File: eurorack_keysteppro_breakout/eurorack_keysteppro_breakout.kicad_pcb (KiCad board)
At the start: 2 copper layers, 25 parts, among them J1 AudioJack2_SwitchT, J10 AudioJack2_SwitchT, J11 AudioJack2_SwitchT, J12 AudioJack2_SwitchT, J13 AudioJack2_SwitchT, J14 AudioJack2_SwitchT, J15 AudioJack2_SwitchT, J16 AudioJack2_SwitchT, J17 AudioJack2_SwitchT, J18 Conn_02x08_Top_Bottom, J19 AudioJack2_SwitchT, J2 AudioJack2_SwitchT, J20 AudioJack2_SwitchT, J21 AudioJack2_SwitchT, J22 AudioJack2_SwitchT, J23 Conn_02x08_Top_Bottom, J24 AudioJack2_SwitchT, J25 AudioJack2_SwitchT, J3 AudioJack2_SwitchT, J4 AudioJack2_SwitchT, J5 AudioJack2_SwitchT, J6 AudioJack2_SwitchT, J7 AudioJack2_SwitchT, J8 AudioJack2_SwitchT, J9 AudioJack2_SwitchT

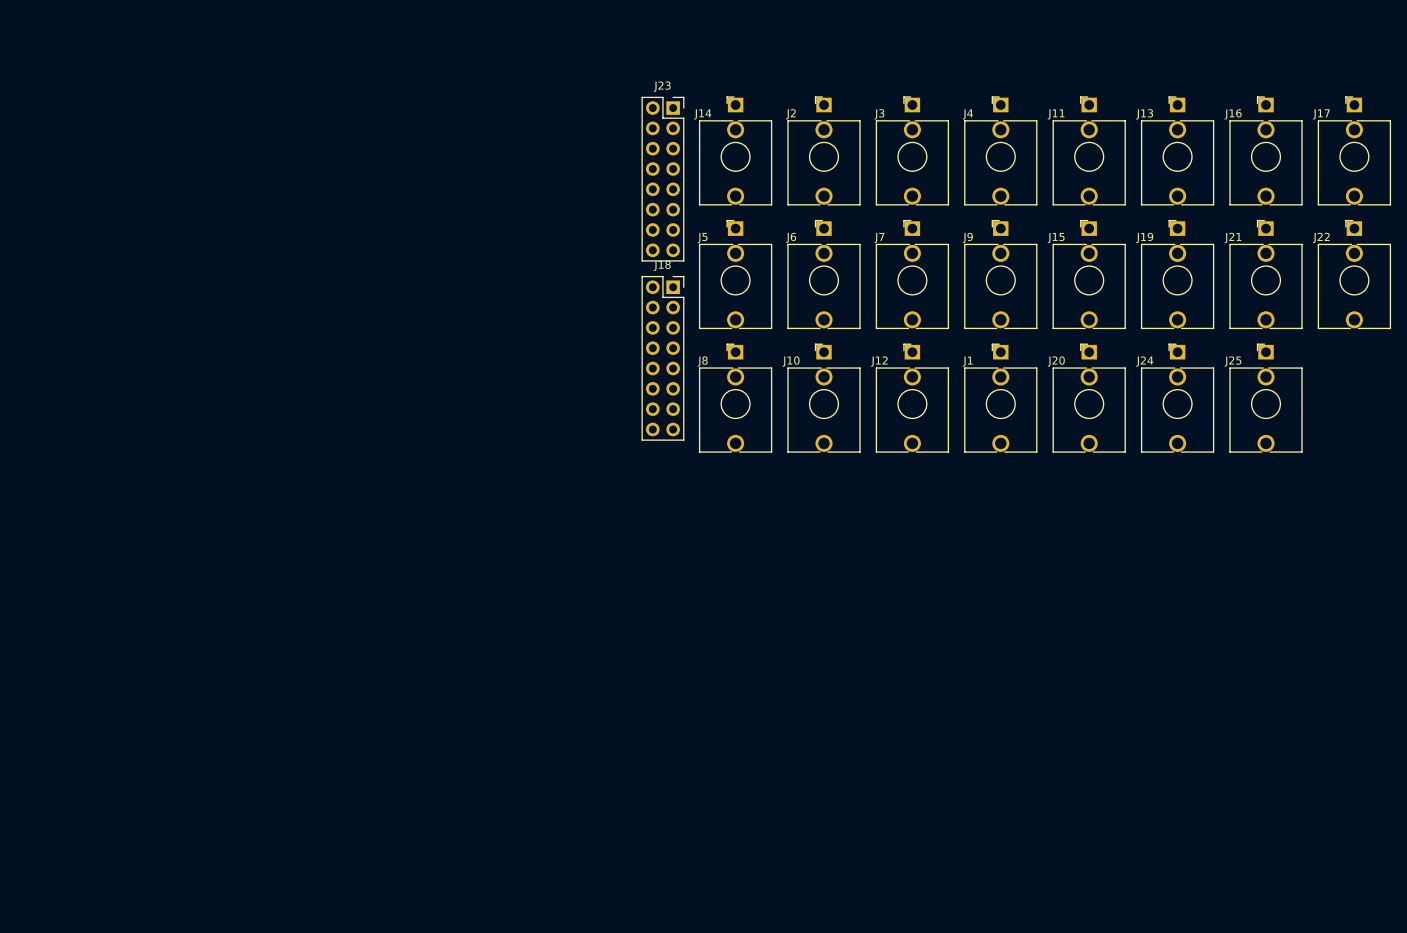
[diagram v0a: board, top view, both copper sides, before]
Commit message: roughly layout connectors
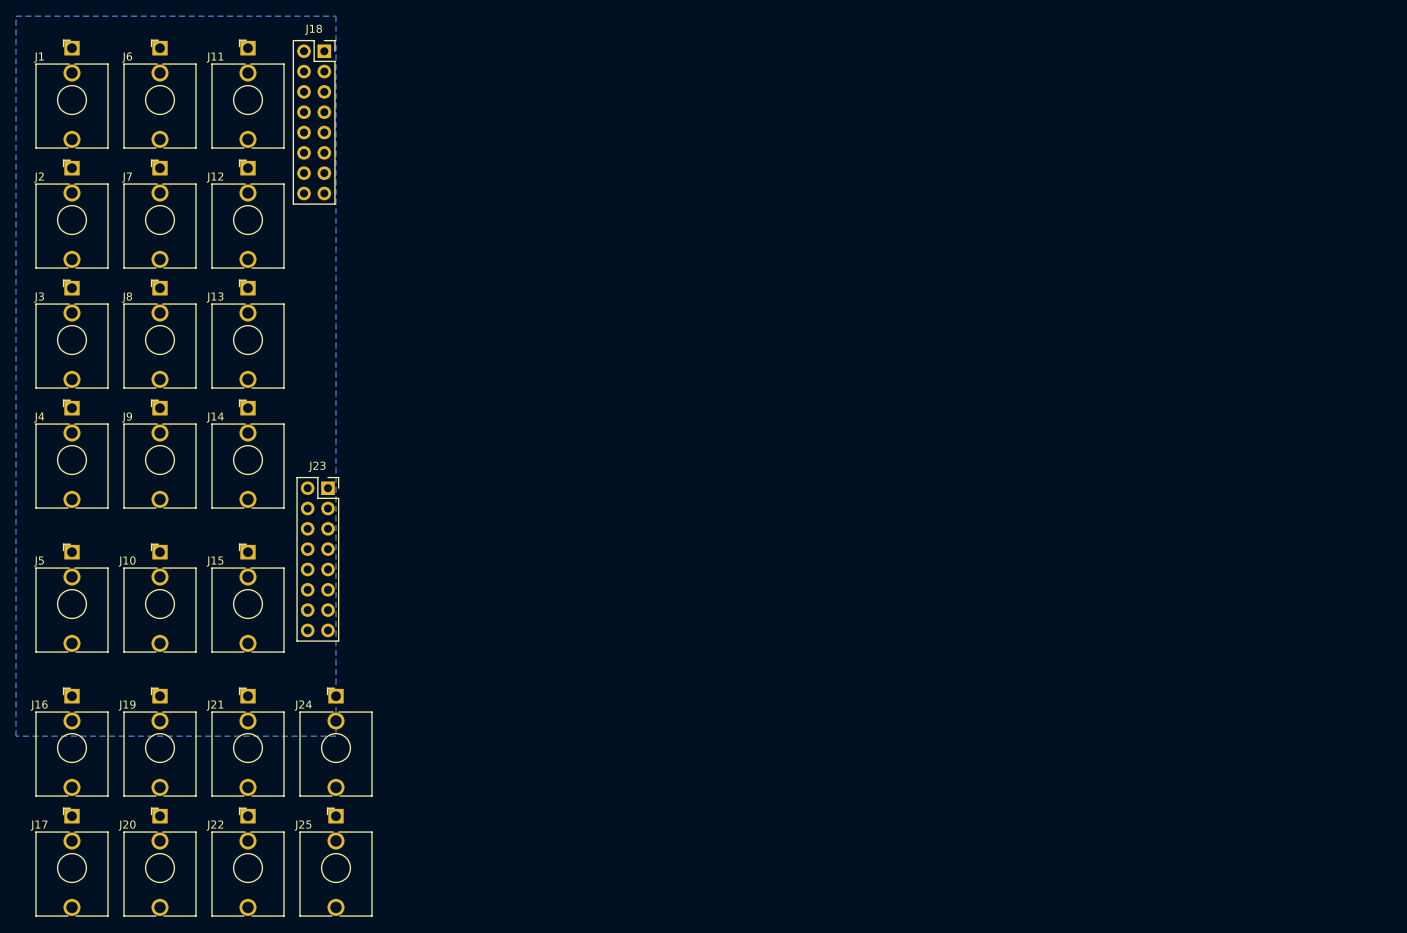
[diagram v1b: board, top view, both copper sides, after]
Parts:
- J1, J10, J11, J12, J13, J14, J15, J16, J17, J19, J2, J20, J21, J22, J24, J25, J3, J4, J5, J6, J7, J8, J9: footprint patchnut:Jack_3.5mm_ThonkiConn_TRS-PJ366ST_Vertical -> Connector_Audio:Jack_3.5mm_QingPu_WQP-PJ398SM_Vertical_CircularHoles
- moved J17 183.3 mm to (47.0, 150.0)
- moved J16 166.5 mm to (47.0, 135.0)
- moved J22 156.6 mm to (69.0, 150.0)
- moved J21 140.0 mm to (69.0, 135.0)
- moved J19 140.0 mm to (58.0, 135.0)
- moved J25 129.9 mm to (80.0, 150.0)
- moved J20 129.8 mm to (58.0, 150.0)
- moved J1 122.2 mm to (47.0, 54.0)
- moved J4 122.1 mm to (47.0, 99.0)
- moved J13 118.4 mm to (69.0, 84.0)
- moved J24 113.6 mm to (80.0, 135.0)
- moved J15 112.7 mm to (69.0, 117.0)
- moved J3 107.5 mm to (47.0, 84.0)
- moved J9 107.5 mm to (58.0, 99.0)
- moved J11 105.4 mm to (69.0, 54.0)
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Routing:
- added copper zone on B.Cu, net GND

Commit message: some layout
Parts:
- J18, J23: value Conn_02x08_Top_Bottom -> Conn_02x08_Odd_Even; footprint Connector_PinSocket_2.54mm:PinSocket_2x08_P2.54mm_Vertical -> Connector_PinHeader_2.54mm:PinHeader_2x08_P2.54mm_Vertical; moved to B.Cu
- moved J5 62.6 mm to (103.0, 145.0)
- moved J10 61.7 mm to (113.0, 145.0)
- moved J15 60.8 mm to (123.0, 145.0)
- moved J4 56.2 mm to (103.0, 94.0)
- moved J3 56.1 mm to (103.0, 80.0)
- moved J2 56.1 mm to (103.0, 66.0)
- moved J1 56.0 mm to (103.0, 52.0)
- moved J9 55.2 mm to (113.0, 94.0)
- moved J8 55.1 mm to (113.0, 80.0)
- moved J7 55.1 mm to (113.0, 66.0)
- moved J6 55.0 mm to (113.0, 52.0)
- moved J14 54.2 mm to (123.0, 94.0)
- moved J13 54.1 mm to (123.0, 80.0)
- moved J17 54.1 mm to (95.0, 125.0)
- moved J12 54.1 mm to (123.0, 66.0)
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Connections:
- J18 pad 1: cv1 -> md2
- J18 pad 10: gt3 -> md4
- J18 pad 11: md3 -> gt3
- J18 pad 12: GND -> gt4
- J18 pad 13: cv4 -> cv3
- J18 pad 14: gt4 -> cv4
- J18 pad 15: md4 -> GND
- J18 pad 2: gt1 -> cv1
- J18 pad 3: md1 -> gt2
- J18 pad 4: GND -> gt1
- J18 pad 6: gt2 -> md1
- J18 pad 7: md2 -> GND
- J18 pad 9: cv3 -> md3
- J23 pad 1: ck_in -> dr6
- J23 pad 10: GND -> (no net)
- J23 pad 11: GND -> ck_out
- J23 pad 12: dr5 -> (no net)
- J23 pad 13: dr6 -> ck_in
- J23 pad 14: GND -> (no net)
- J23 pad 15: dr7 -> ck_rst
- J23 pad 16: dr8 -> (no net)
- J23 pad 2: ck_rst -> dr3
- J23 pad 3: GND -> dr2
- J23 pad 4: dr1 -> dr7
- J23 pad 5: dr2 -> dr5
- J23 pad 6: GND -> dr4
- J23 pad 7: dr3 -> dr1
- J23 pad 8: dr4 -> dr8
- J23 pad 9: ck_out -> GND
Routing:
- net ck_rst: track 0.00 -> 29.3 mm
- net ck_out: track 0.00 -> 19.5 mm
- net ck_in: track 0.00 -> 8.48 mm
- added copper zone on F.Cu, net GND
- removed copper zone on B.Cu, net GND
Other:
- board outline added: 40 x 110 mm

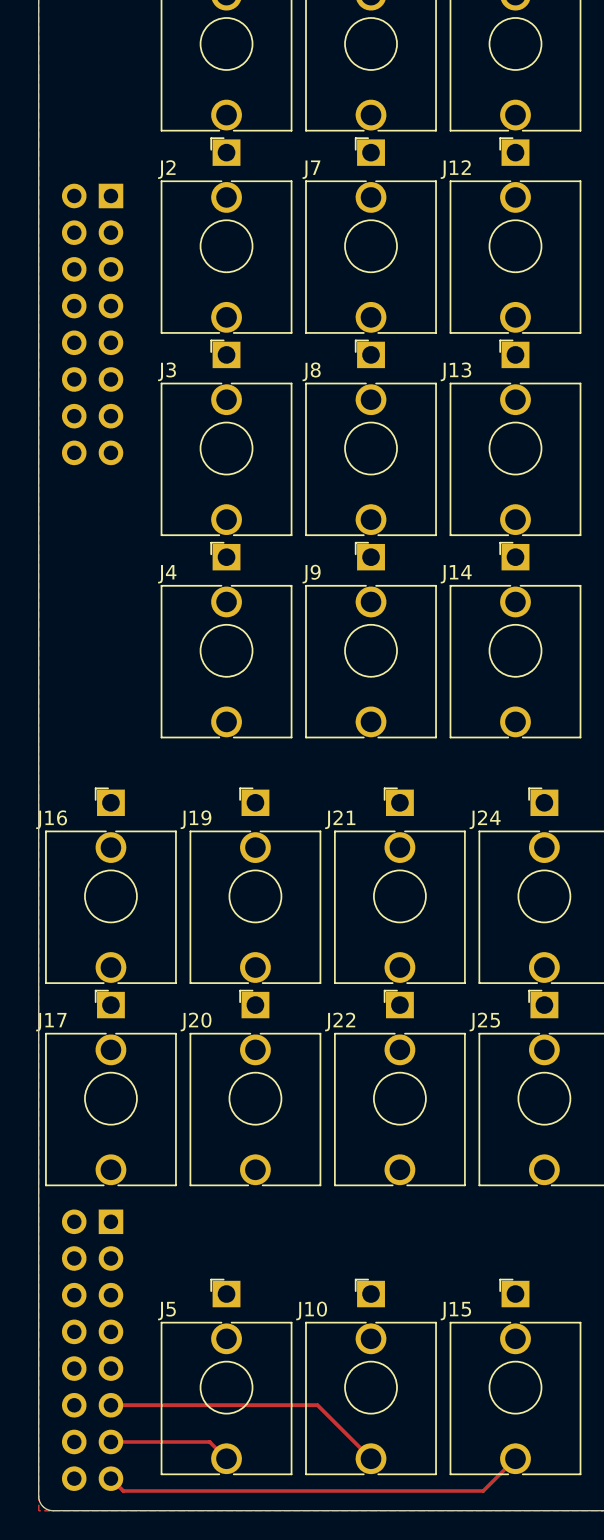
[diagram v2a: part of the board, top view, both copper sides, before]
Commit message: route traces for gate/trigger/mod and clock signals
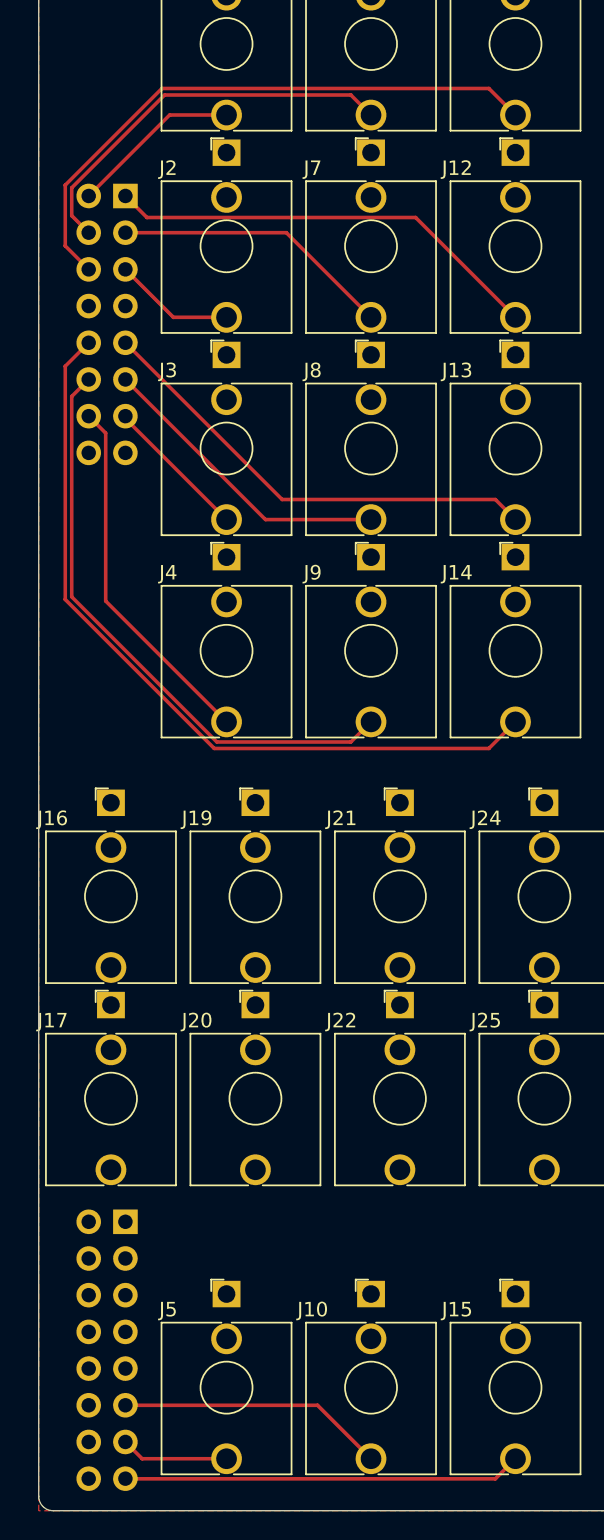
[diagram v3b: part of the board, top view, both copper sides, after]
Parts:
- moved J18 1.00 mm to (96.0, 69.0)
- moved J23 1.00 mm to (96.0, 140.0)
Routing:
- net md4: track 0.00 -> 54.6 mm
- net md1: track 0.00 -> 41.2 mm
- net gt4: track 0.00 -> 41.0 mm
- net md3: track 0.00 -> 32.1 mm
- net md2: track 0.00 -> 30.5 mm
- net gt1: track 0.00 -> 27.5 mm
- net cv4: track 0.00 -> 25.1 mm
- net gt3: track 0.00 -> 21.0 mm
- net gt2: track 0.00 -> 19.4 mm
- net cv1: track 0.00 -> 11.9 mm
- net cv3: track 0.00 -> 10.1 mm
- net cv2: track 0.00 -> 8.38 mm
- net ck_rst: track 29.3 -> 27.6 mm
- net ck_out: track 19.5 -> 18.5 mm
- net ck_in: track 8.48 -> 7.48 mm

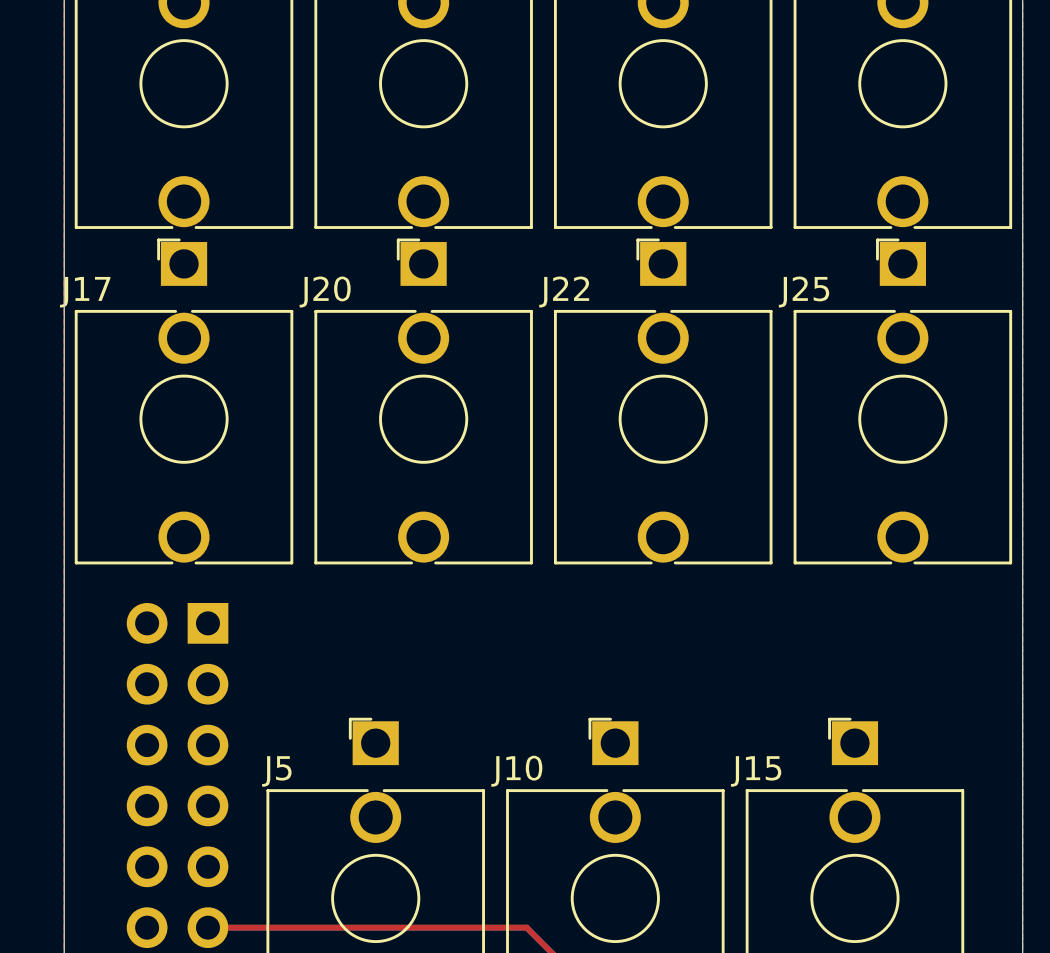
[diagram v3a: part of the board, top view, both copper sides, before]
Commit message: reorder pins on clock and trigger header, route the rest of the tracks
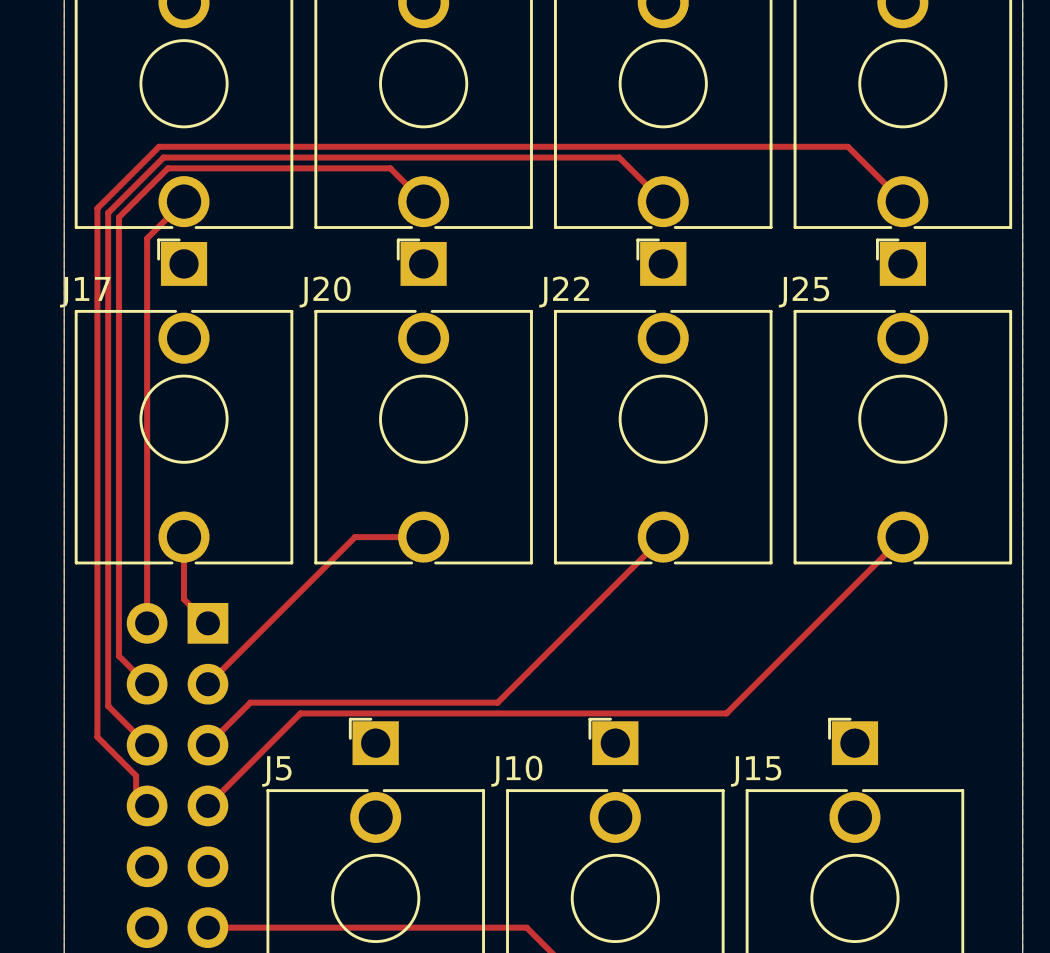
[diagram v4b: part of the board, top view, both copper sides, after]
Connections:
- J23 pad 1: dr6 -> dr5
- J23 pad 2: dr3 -> dr1
- J23 pad 3: dr2 -> dr6
- J23 pad 4: dr7 -> dr2
- J23 pad 5: dr5 -> dr7
- J23 pad 6: dr4 -> dr3
- J23 pad 7: dr1 -> dr8
- J23 pad 8: dr8 -> dr4
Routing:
- net dr4: track 0.00 -> 61.4 mm
- net dr3: track 0.00 -> 47.8 mm
- net dr2: track 0.00 -> 34.1 mm
- net dr8: track 0.00 -> 33.6 mm
- net dr7: track 0.00 -> 22.6 mm
- net dr1: track 0.00 -> 18.2 mm
- net dr6: track 0.00 -> 11.5 mm
- net dr5: track 0.00 -> 4.01 mm
